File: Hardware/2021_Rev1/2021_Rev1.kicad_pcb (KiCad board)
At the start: 2 copper layers, 28 parts, among them J1 USB_A, U1 TM4C129E_Launchpad, U2 OKI, U3 OKI, U4 FT230XS

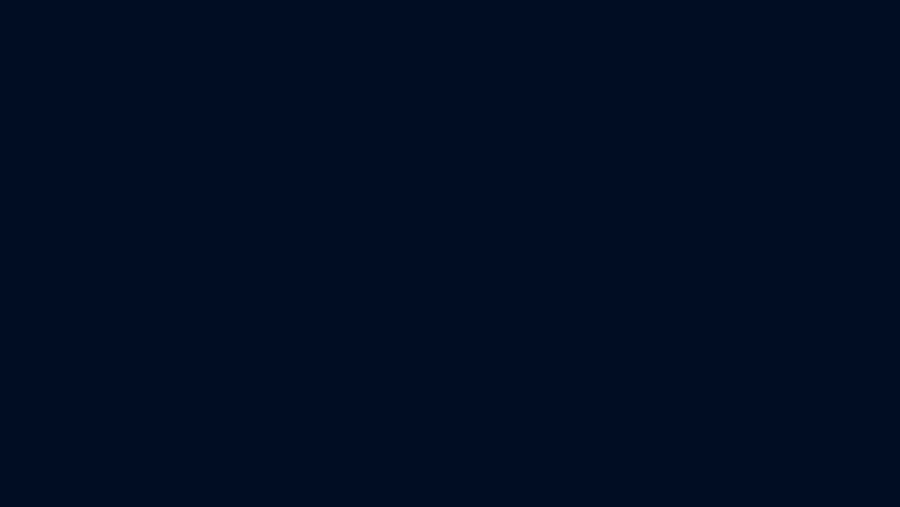
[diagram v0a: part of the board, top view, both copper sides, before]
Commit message: Updated Schematic and Layout
Changed joystick pins from GND to 3.3V and updated USB circuit to a known working circuit
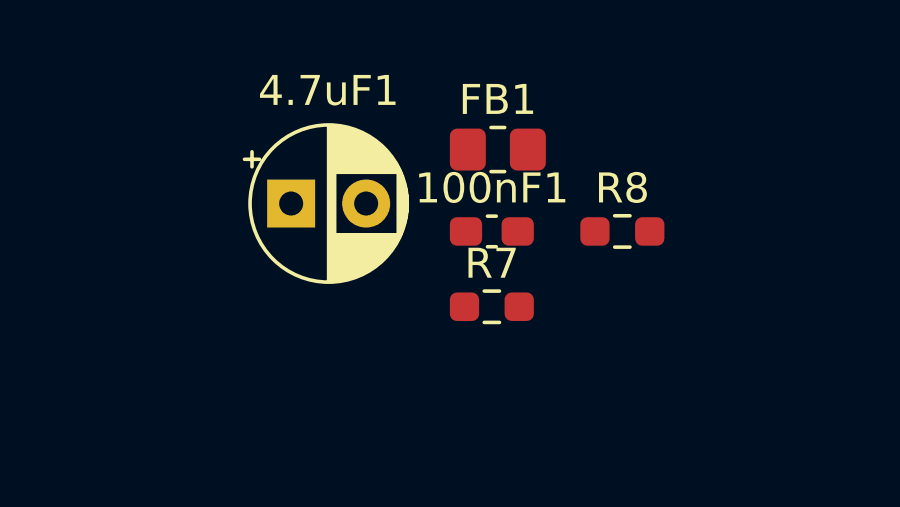
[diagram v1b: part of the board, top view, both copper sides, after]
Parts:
- added 100nF1: C_Small, Capacitor_SMD:C_0603_1608Metric_Pad1.08x0.95mm_HandSolder, F.Cu at (941.8, -261.7)
- added 4.7uF1: C_Polarized_Small_US, Capacitor_THT:CP_Radial_D5.0mm_P2.50mm, F.Cu at (935.1, -262.7)
- added FB1: MI0805K601R-10, Resistor_SMD:R_0805_2012Metric_Pad1.20x1.40mm_HandSolder, F.Cu at (942.0, -264.5)
- added R7: 330, Resistor_SMD:R_0603_1608Metric_Pad0.98x0.95mm_HandSolder, F.Cu at (941.8, -259.2)
- added R8: 330, Resistor_SMD:R_0603_1608Metric_Pad0.98x0.95mm_HandSolder, F.Cu at (946.1, -261.7)
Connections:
- Conn3 pad 1: GND -> +3V3
- Conn3 pad 2: GND -> +3V3
- Conn3 pad 3: GND -> +3V3
- Conn3 pad 4: GND -> +3V3
- Conn4 pad 1: ELEV_CTL -> Net-(Conn4-Pad1)
- Conn5 pad 1: AZI_CTL -> Net-(Conn5-Pad1)
- J1 pad 1: +5V -> Net-(FB1-Pad2)
- J1 pad 5: GND -> Net-(J1-Pad5)
- U4 pad 12: +5V -> Net-(100nF1-Pad1)

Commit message: Finished Layout
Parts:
- added D3: BLUE, LED_SMD:LED_0603_1608Metric_Pad1.05x0.95mm_HandSolder, F.Cu at (958.3, -224.7)
- added D4: BLUE, LED_SMD:LED_0603_1608Metric_Pad1.05x0.95mm_HandSolder, F.Cu at (955.3, -224.7)
- added D5: BLUE, LED_SMD:LED_0603_1608Metric_Pad1.05x0.95mm_HandSolder, F.Cu at (955.3, -233.6)
- added D6: BLUE, LED_SMD:LED_0603_1608Metric_Pad1.05x0.95mm_HandSolder, F.Cu at (958.3, -233.5)
- added D7: BLUE, LED_SMD:LED_0603_1608Metric_Pad1.05x0.95mm_HandSolder, F.Cu at (961.6, -233.6)
- added D8: BLUE, LED_SMD:LED_0603_1608Metric_Pad1.05x0.95mm_HandSolder, F.Cu at (964.7, -233.6)
- added R10: 330, Resistor_SMD:R_0603_1608Metric_Pad0.98x0.95mm_HandSolder, F.Cu at (958.3, -229.5)
- added R11: 330, Resistor_SMD:R_0603_1608Metric_Pad0.98x0.95mm_HandSolder, F.Cu at (961.6, -229.5)
- added R12: 330, Resistor_SMD:R_0603_1608Metric_Pad0.98x0.95mm_HandSolder, F.Cu at (964.7, -229.5)
- added R9: 330, Resistor_SMD:R_0603_1608Metric_Pad0.98x0.95mm_HandSolder, F.Cu at (955.3, -229.5)
- BT1: moved to F.Cu
- D1, D2: value PINK -> BLUE
- U1: moved to B.Cu
- moved Conn5 105.1 mm to (941.1, -219.7)
- moved C2 93.8 mm to (966.1, -207.0)
- moved Conn7 87.4 mm to (943.6, -237.5)
- moved Conn4 82.5 mm to (928.4, -228.6)
- moved Conn6 81.2 mm to (913.1, -237.5)
- moved 4.7uF1 81.0 mm to (1009.1, -229.9)
- moved C6 79.1 mm to (978.3, -229.6), turned to 180 degrees
- moved 100nF1 78.4 mm to (1010.1, -223.3)
- moved Conn3 78.2 mm to (913.1, -228.6)
- moved C3 77.7 mm to (984.2, -190.9), turned to 270 degrees
- moved U3 77.2 mm to (984.2, -196.8), turned to 90 degrees
- moved C4 76.4 mm to (985.1, -207.0)
- moved C5 75.1 mm to (982.1, -229.6)
- moved D1 75.1 mm to (986.1, -218.2), turned to 180 degrees
- moved Conn8 69.5 mm to (928.4, -219.7)
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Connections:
- 100nF1 pad 1: Net-(100nF1-Pad1) -> +5V
- 4.7uF1 pad 1: Net-(100nF1-Pad1) -> +5V
- Conn4 pad 1: Net-(Conn4-Pad1) -> ELEV_CTL
- Conn5 pad 1: Net-(Conn5-Pad1) -> AZI_CTL
- FB1 pad 1: Net-(100nF1-Pad1) -> +5V
- J1 pad 5: Net-(J1-Pad5) -> GND
- R7 pad 1: Net-(Conn5-Pad1) -> Net-(D4-Pad2)
- R8 pad 1: Net-(Conn4-Pad1) -> Net-(D3-Pad2)
- U4 pad 12: Net-(100nF1-Pad1) -> +5V
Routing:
- net +3V3: track 0.00 -> 101.8 mm, vias 0 -> 2
- net +5V: track 0.00 -> 81.8 mm, vias 0 -> 5
- net ELEV_PLUS: track 0.00 -> 68.4 mm, vias 0 -> 1
- net ELEV_CTL: track 0.00 -> 64.0 mm, vias 0 -> 3
- net ELEV_MINUS: track 0.00 -> 63.4 mm, vias 0 -> 1
- net AZI_PLUS: track 0.00 -> 57.3 mm, vias 0 -> 1
- net AZI_MINUS: track 0.00 -> 52.1 mm, vias 0 -> 1
- net +9V: track 0.00 -> 40.6 mm
- net AZI_CTL: track 0.00 -> 37.4 mm, vias 0 -> 2
- net KBoard_TX: track 0.00 -> 25.9 mm, vias 0 -> 2
- net KBoard_RX: track 0.00 -> 24.7 mm
- net Net-(R1-Pad1): track 0.00 -> 22.9 mm, vias 0 -> 3
- net LCD_TX: track 0.00 -> 21.8 mm, vias 0 -> 1
- net Net-(R2-Pad1): track 0.00 -> 16.9 mm, vias 0 -> 2
- net Net-(C7-Pad1): track 0.00 -> 9.95 mm
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- added copper zone on B.Cu, net (none)
- added copper zone on F.Cu, net GND
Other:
- board outline added: 124.5 x 81.3 mm

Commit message: Added Signature
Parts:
- added G***: LOGO, MRDT_Silkscreens:0_MRDT_Logo_10mm, F.Cu at (1012.4, -181.6)
- added G***: LOGO, Packages:Signature_15mm_Esther, F.Cu at (902.5, -220.5)
- added REF**: 4_40_Hole, MRDT_Drill_Holes:4_40_Hole_Corner, F.Cu at (1013.0, -237.0)
- added REF**: 4_40_Hole, MRDT_Drill_Holes:4_40_Hole_Corner, F.Cu at (1013.0, -172.0)
- added REF**: 4_40_Hole, MRDT_Drill_Holes:4_40_Hole_Corner, F.Cu at (904.7, -172.0)
- added REF**: 4_40_Hole, MRDT_Drill_Holes:4_40_Hole_Corner, F.Cu at (904.7, -237.0)

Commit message: tiva footprint changed to THT_BOTTOM
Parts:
- removed G***: LOGO, MRDT_Silkscreens:0_MRDT_Logo_10mm
- removed G***: LOGO, Packages:Signature_15mm_Esther
- removed REF** (x4): 4_40_Hole, MRDT_Drill_Holes:4_40_Hole_Corner
- U1: footprint MRDT_Shields:TM4C129E_Launchpad_FULL_THT_TOP -> MRDT_Shields:TM4C129E_Launchpad_FULL_THT_BOTTOM; moved to F.Cu
- moved U1 89.9 mm to (996.7, -213.4), turned to 180 degrees
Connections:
- J1 pad 5: GND -> Net-(J1-Pad5)
- J1 pad e5: GND -> (no net)
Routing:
- net LCD_TX: track 21.8 -> 5.84 mm
- net AZI_CTL: track 37.4 -> 24.6 mm
- net +3V3: track 101.8 -> 90.4 mm
- net ELEV_MINUS: track 63.4 -> 53.9 mm
- net AZI_PLUS: track 57.3 -> 47.8 mm
- net AZI_MINUS: track 52.1 -> 42.6 mm
- net ELEV_PLUS: track 68.4 -> 59.1 mm
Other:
- board text added: "Equipment Servicing Panel, Rev1 Mars Rover Design Team Missouri S&T, 2021 Esther Warren"

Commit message: Revert "tiva footprint changed to THT_BOTTOM"
This reverts commit b87381c65a80fcd5fad75ae35fe4b21bdfbb7d2f.
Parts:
- added G***: LOGO, MRDT_Silkscreens:0_MRDT_Logo_10mm, F.Cu at (1012.4, -181.6)
- added G***: LOGO, Packages:Signature_15mm_Esther, F.Cu at (902.5, -220.5)
- added REF**: 4_40_Hole, MRDT_Drill_Holes:4_40_Hole_Corner, F.Cu at (1013.0, -237.0)
- added REF**: 4_40_Hole, MRDT_Drill_Holes:4_40_Hole_Corner, F.Cu at (1013.0, -172.0)
- added REF**: 4_40_Hole, MRDT_Drill_Holes:4_40_Hole_Corner, F.Cu at (904.7, -172.0)
- added REF**: 4_40_Hole, MRDT_Drill_Holes:4_40_Hole_Corner, F.Cu at (904.7, -237.0)
- U1: footprint MRDT_Shields:TM4C129E_Launchpad_FULL_THT_BOTTOM -> MRDT_Shields:TM4C129E_Launchpad_FULL_THT_TOP; moved to B.Cu
- moved U1 89.9 mm to (906.8, -213.4), turned to 0 degrees
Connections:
- J1 pad 5: Net-(J1-Pad5) -> GND
- J1 pad e5: (no net) -> GND
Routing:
- net LCD_TX: track 5.84 -> 21.8 mm
- net AZI_CTL: track 24.6 -> 37.4 mm
- net +3V3: track 90.4 -> 101.8 mm
- net ELEV_MINUS: track 53.9 -> 63.4 mm
- net AZI_PLUS: track 47.8 -> 57.3 mm
- net AZI_MINUS: track 42.6 -> 52.1 mm
- net ELEV_PLUS: track 59.1 -> 68.4 mm
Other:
- board text removed: "Equipment Servicing Panel, Rev1 Mars Rover Design Team Missouri S&T, 2021 Esther Warren"

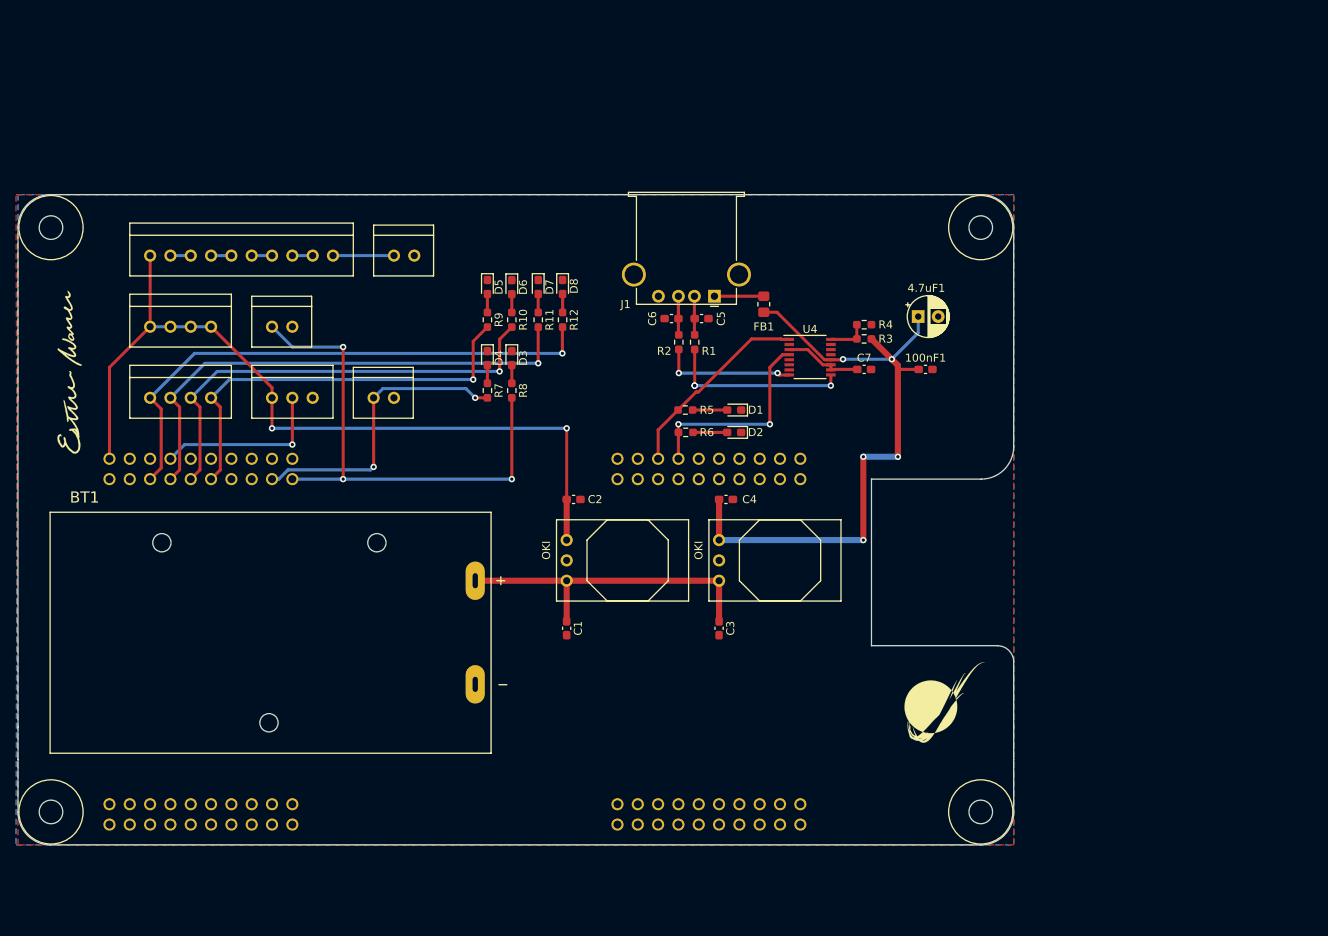
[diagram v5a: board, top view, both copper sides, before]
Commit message: nvm we did a jank fix
changing the footprint broke everything so we just flipped the board and then flipped the tiva to the front.
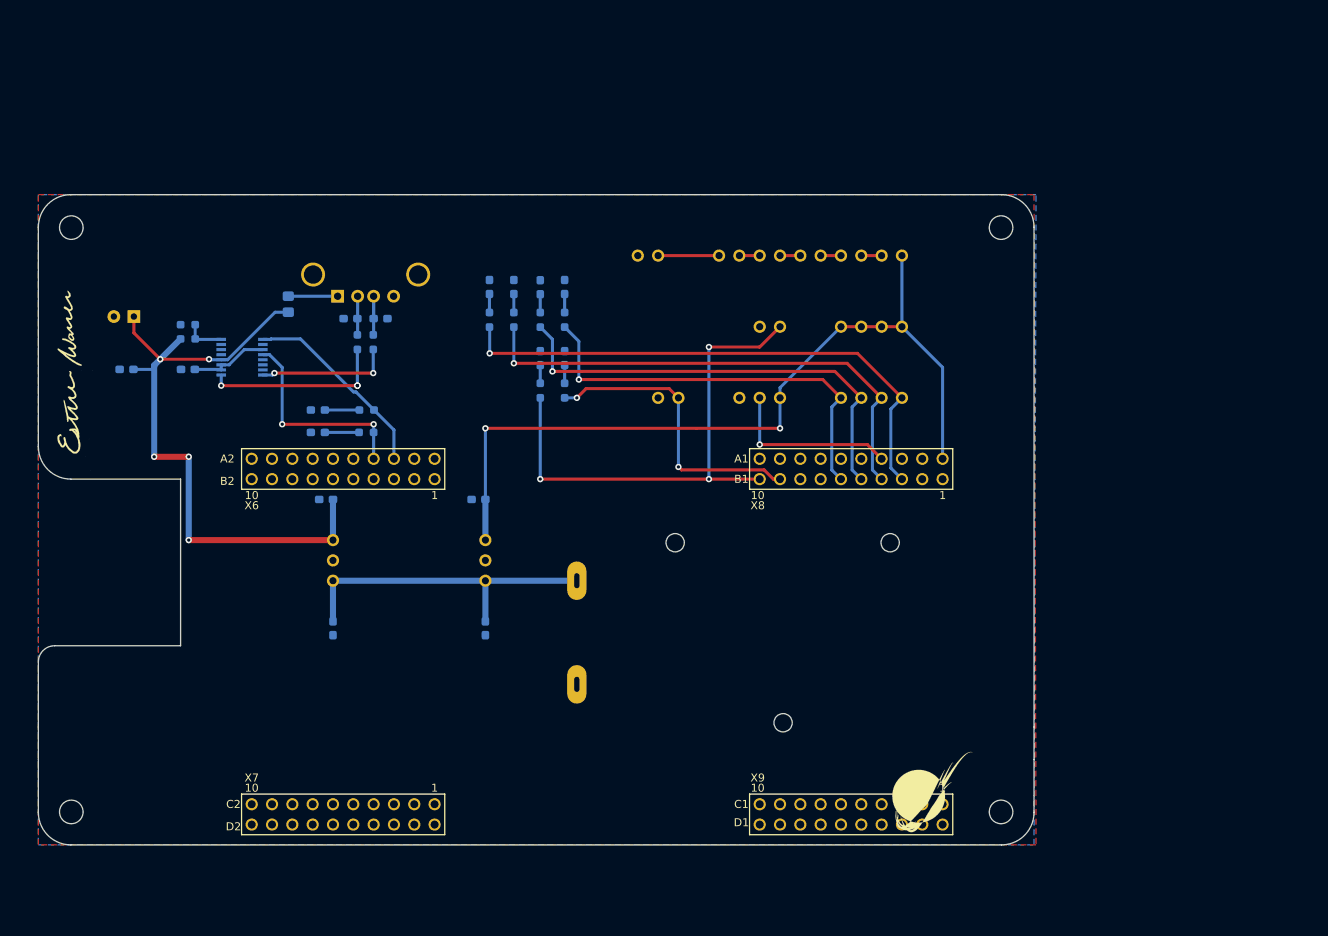
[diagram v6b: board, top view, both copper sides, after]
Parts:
- 100nF1, 4.7uF1, BT1, C1, C2, C3, C4, C5, C6, C7, Conn2, Conn3, Conn4, Conn5, Conn6, Conn7, Conn8, D1, D2, D3, D4, D5, D6, D7, D8, FB1, J1, R1, R10, R11, R12, R2, R3, R4, R5, R6, R7, R8, R9, REF** (x4), U2, U3, U4: moved to B.Cu
- U1: moved to F.Cu
- moved REF** 110.7 mm to (1015.5, -172.0), turned to 0 degrees
- moved REF** 110.7 mm to (1015.5, -237.0)
- moved U1 106.7 mm to (1013.5, -213.4), turned to 180 degrees
- moved REF** 105.7 mm to (907.3, -237.0), turned to 180 degrees
- moved REF** 105.7 mm to (907.3, -172.0)
- moved 100nF1 99.9 mm to (910.2, -223.3), turned to 180 degrees
- moved 4.7uF1 98.0 mm to (911.1, -229.9), turned to 180 degrees
- moved Conn2 94.0 mm to (1007.1, -219.7), turned to 180 degrees
- moved Conn3 94.0 mm to (1007.1, -228.6), turned to 180 degrees
- moved Conn6 94.0 mm to (1007.1, -237.5), turned to 180 degrees
- moved R3 84.5 mm to (917.9, -227.1), turned to 0 degrees
- moved R4 84.5 mm to (917.9, -228.9), turned to 180 degrees
- moved C7 84.5 mm to (917.9, -223.3), turned to 180 degrees
- moved U4 71.0 mm to (924.6, -224.8), turned to 180 degrees
- moved BT1 64.3 mm to (992.3, -190.4), turned to 180 degrees
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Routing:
- added copper zone on F.Cu, net (none)
- added copper zone on B.Cu, net GND
- removed copper zone on B.Cu, net (none)
- removed copper zone on F.Cu, net GND
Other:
- outline, holes or cut-outs redrawn

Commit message: Layout Finished
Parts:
- G*** (x2): moved to B.Cu
- moved G*** 100.1 mm to (911.4, -180.3), turned to 180 degrees
- moved G*** 55.2 mm to (936.5, -177.0), turned to 180 degrees
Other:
- board text added: "AZI +"
- board text added: "AZI -"
- board text added: "AZI CTL"
- board text added: "ELEV +"
- board text added: "ELEV -"
- board text added: "ELEV CTL"
- board text added: "Epuipment Servicing Panel Mars Rover Design Team Missouri S&T, 2020 Esther Warren"
- board text added: "KBoard RX"
- board text added: "KBoard_TX"
